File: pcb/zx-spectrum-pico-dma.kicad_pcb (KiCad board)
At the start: 2 copper layers, 98.2 x 99.9 mm, 19 parts, among them J101 SWD, J102 Blippers, J103 Z80 Data Bus, J104 Z80 Address Bus, J105 Z80 Control Bus, J106 ZX Control, J107 OLED, J108 Spare GPIOs, Q101 PMBT2222A, SW101 BTN_RESET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

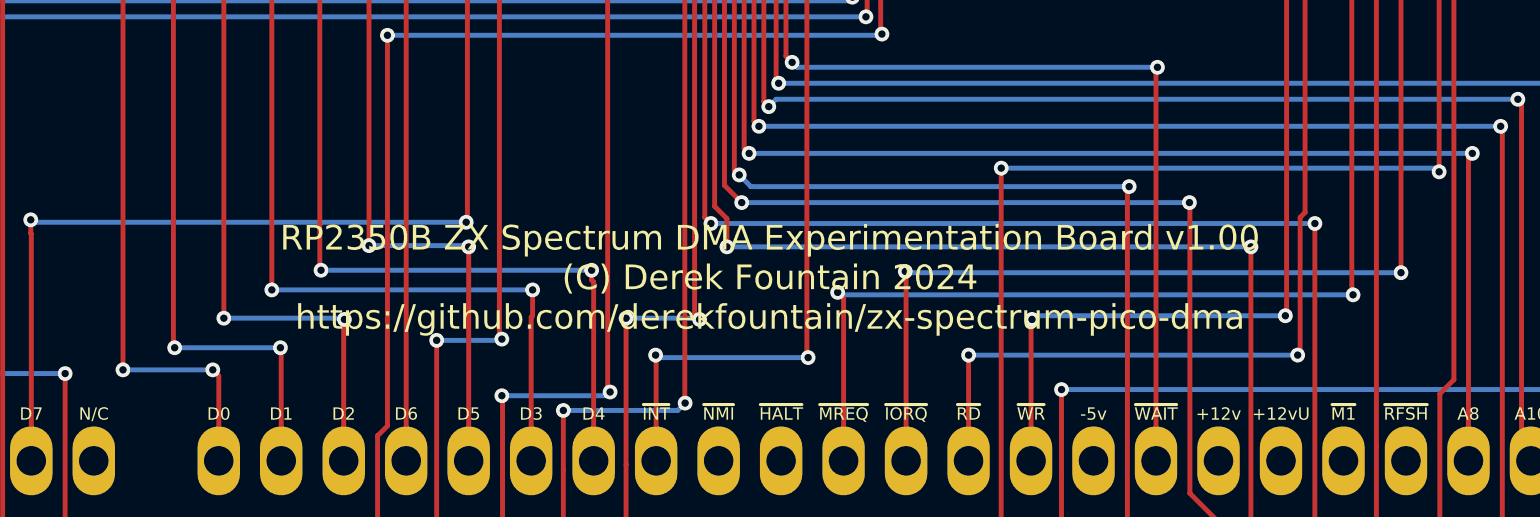
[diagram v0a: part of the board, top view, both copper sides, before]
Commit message: update schematic to reflect the revised RESET labelling
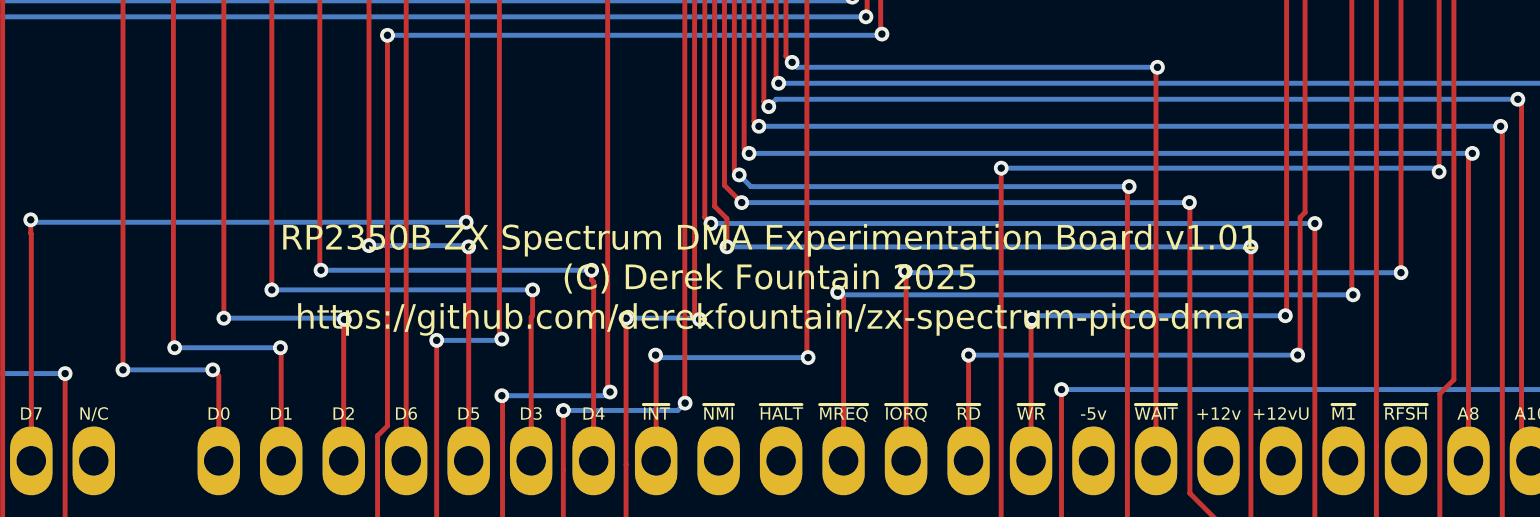
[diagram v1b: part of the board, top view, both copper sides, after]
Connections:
- net /RESET_Z80 renamed RESET_Z80
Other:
- board text added: "RP2350B ZX Spectrum DMA Experimentation Board v1.01 (C) Derek Fountain 2025 https://github.com/derekfountain/zx-spectrum-pico-dma"
- board text removed: "RP2350B ZX Spectrum DMA Experimentation Board v1.00 (C) Derek Fountain 2024 https://github.com/derekfountain/zx-spectrum-pico-dma"

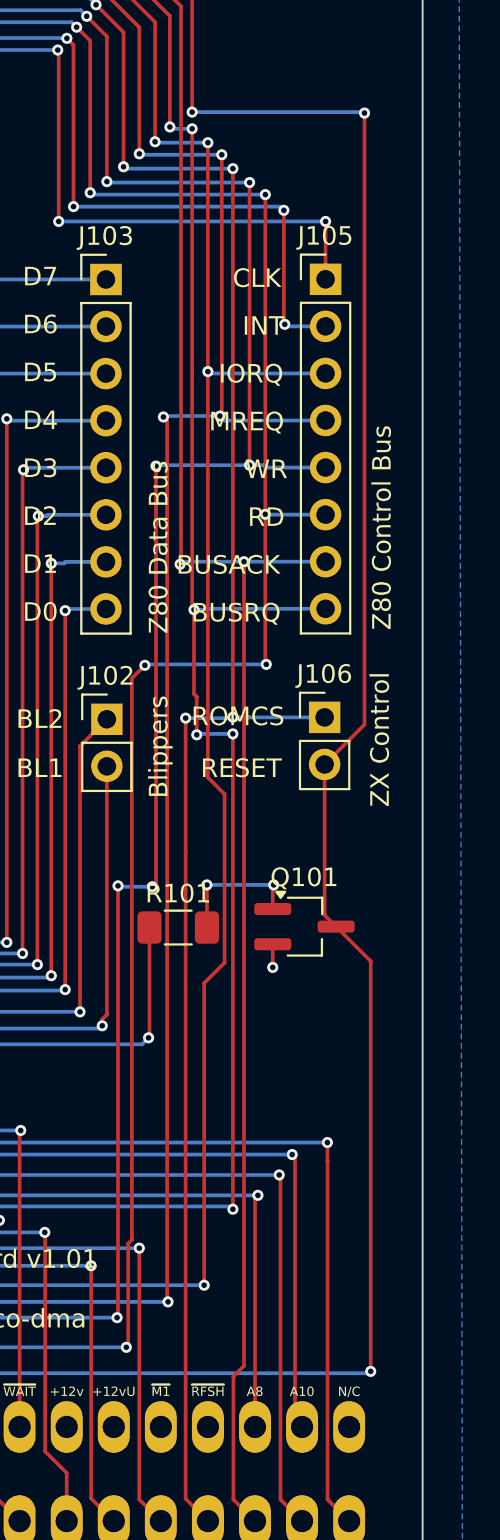
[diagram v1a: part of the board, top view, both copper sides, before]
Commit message: add M1 from edge connector to a pin, it's needed on the logic analyser so I need to make it available
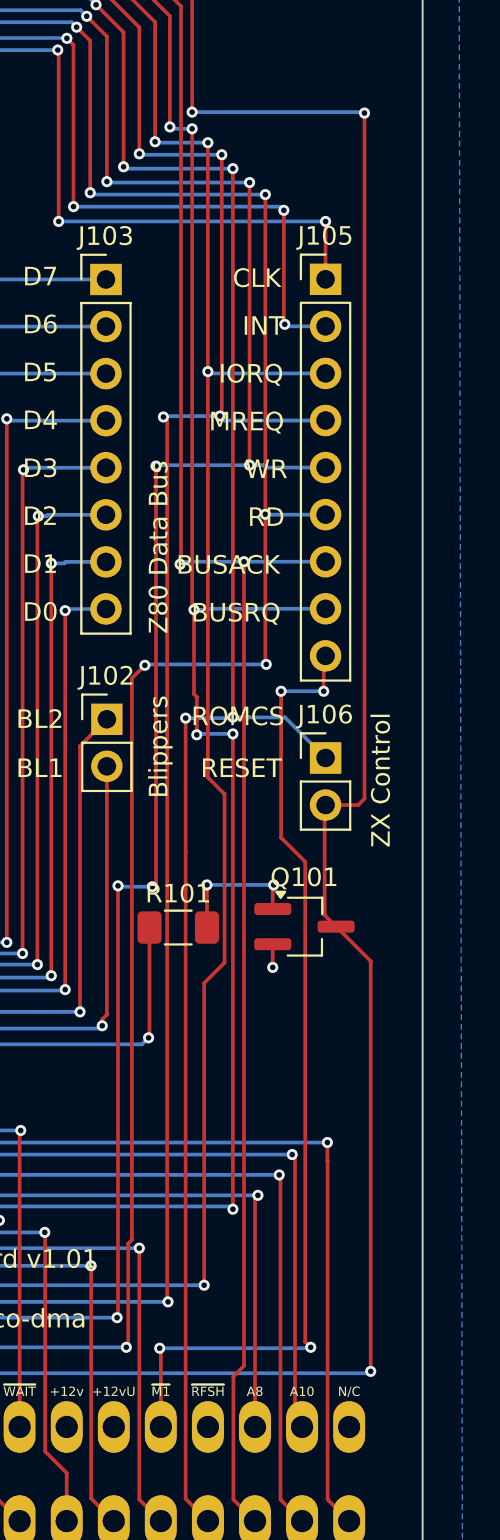
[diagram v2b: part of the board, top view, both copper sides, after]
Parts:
- J105: value Z80 Control Bus -> Conn_01x09; footprint Connector_PinHeader_2.54mm:PinHeader_1x08_P2.54mm_Vertical -> Connector_PinHeader_2.54mm:PinHeader_1x09_P2.54mm_Vertical
- moved J106 2.19 mm to (144.6, 108.8)
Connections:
- Z101 pad A24: unconnected-(Z101-~{M1}-PadA24) -> ZXM1
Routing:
- net ZXM1: track 0.00 -> 52.8 mm, vias 0 -> 4
- net ZXRESET: track 169.7 -> 170.7 mm
- net ZXROMCS: track 129.7 -> 130.7 mm
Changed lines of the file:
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@@
 	(paper "A4")
 	(title_block
-		(date "2024-11-29")
+		(date "2025-03-14")
 	)
 	(layers
@@
 	(net 68 "unconnected-(Z101-NC-PadA28)")
 	(net 69 "/GPIO39")
-	(net 70 "unconnected-(Z101-~{M1}-PadA24)")
+	(net 70 "ZXM1")
 	(net 71 "unconnected-(Z101-~{NMI}-PadA14)")
 	(net 72 "unconnected-(Z101-~{HALT}-PadA15)")
@@
 	(footprint "Connector_PinHeader_2.54mm:PinHeader_1x02_P2.54mm_Vertical"
 		(layer "F.Cu")
-		(at 144.5 106.66)
+		(at 144.55 108.85)
 		(descr "Through hole straight pin header, 1x02, 2.54mm pitch, single row")
 		(tags "Through hole pin header THT 1x02 2.54mm single row")
@@
 			)
 			(remove_unused_layers no)
-			(net 70 "unconnected-(Z101-~{M1}-PadA24)")
+			(net 70 "ZXM1")
 			(pinfunction "~{M1}")
-			(pintype "input+no_connect")
+			(pintype "input")
 		)
 		(pad "A25" thru_hole oval
@@
 		)
 	)
-	(footprint "Connector_PinHeader_2.54mm:PinHeader_1x08_P2.54mm_Vertical"
+	(footprint "Connector_PinHeader_2.54mm:PinHeader_1x09_P2.54mm_Vertical"
 		(layer "F.Cu")
 		(at 144.55 83.02)
-		(descr "Through hole straight pin header, 1x08, 2.54mm pitch, single row")
-		(tags "Through hole pin header THT 1x08 2.54mm single row")
+		(descr "Through hole straight pin header, 1x09, 2.54mm pitch, single row")
+		(tags "Through hole pin header THT 1x09 2.54mm single row")
 		(property "Reference" "J105"
 			(at 0 -2.33 0)
@@
 			)
 		)
-		(property "Value" "Z80 Control Bus"
-			(at 3.05 13.4 90)
-			(layer "F.SilkS")
+		(property "Value" "Conn_01x09"
+			(at 0 22.65 0)
+			(layer "F.Fab")
 			(effects
 				(font
@@
 			)
 		)
-		(property "Footprint" "Connector_PinHeader_2.54mm:PinHeader_1x08_P2.54mm_Vertical"
+		(property "Footprint" "Connector_PinHeader_2.54mm:PinHeader_1x09_P2.54mm_Vertical"
 			(at 0 0 0)
 			(unlocked yes)
@@
 			)
 		)
-		(property "Description" "Generic connector, single row, 01x08, script generated (kicad-library-utils/schlib/autogen/connector/)"
+		(property "Description" "Generic connector, single row, 01x09, script generated (kicad-library-utils/schlib/autogen/connector/)"
 			(at 0 0 0)
 			(unlocked yes)
@@
 		(fp_line
 			(start -1.33 1.27)
-			(end -1.33 19.11)
+			(end -1.33 21.65)
 			(stroke
 				(width 0.12)
@@
 		)
 		(fp_line
-			(start -1.33 19.11)
-			(end 1.33 19.11)
+			(start -1.33 21.65)
+			(end 1.33 21.65)
 			(stroke
 				(width 0.12)
@@
 		(fp_line
 			(start 1.33 1.27)
-			(end 1.33 19.11)
+			(end 1.33 21.65)
 			(stroke
 				(width 0.12)
@@
 		(fp_line
 			(start -1.8 -1.8)
-			(end -1.8 19.55)
+			(end -1.8 22.1)
 			(stroke
 				(width 0.05)
@@
 		)
 		(fp_line
-			(start -1.8 19.55)
-			(end 1.8 19.55)
+			(start -1.8 22.1)
+			(end 1.8 22.1)
 			(stroke
 				(width 0.05)
@@
 		)
 		(fp_line
-			(start 1.8 19.55)
+			(start 1.8 22.1)
 			(end 1.8 -1.8)
 			(stroke
@@
 		)
 		(fp_line
-			(start -1.27 19.05)
+			(start -1.27 21.59)
 			(end -1.27 -0.635)
 			(stroke
@@
 		(fp_line
 			(start 1.27 -1.27)
-			(end 1.27 19.05)
+			(end 1.27 21.59)
 			(stroke
 				(width 0.1)
@@
 		)
 		(fp_line
-			(start 1.27 19.05)
-			(end -1.27 19.05)
+			(start 1.27 21.59)
+			(end -1.27 21.59)
 			(stroke
 				(width 0.1)
@@
 		)
 		(fp_text user "${REFERENCE}"
-			(at 0 8.89 90)
+			(at 0 10.16 90)
 			(layer "F.Fab")
 			(effects
@@
 			(pintype "passive")
 		)
-		(model "${KICAD8_3DMODEL_DIR}/Connector_PinHeader_2.54mm.3dshapes/PinHeader_1x08_P2.54mm_Vertical.wrl"
+		(pad "9" thru_hole oval
+			(at 0 20.32)
+			(size 1.7 1.7)
+			(drill 1)
+			(layers "*.Cu" "*.Mask" "In1.Cu" "In2.Cu" "In3.Cu" "In4.Cu" "In5.Cu" "In6.Cu"
+				"In7.Cu" "In8.Cu" "In9.Cu" "In10.Cu" "In11.Cu" "In12.Cu" "In13.Cu" "In14.Cu"
+				"In15.Cu" "In16.Cu" "In17.Cu" "In18.Cu" "In19.Cu" "In20.Cu" "In21.Cu"
+				"In22.Cu" "In23.Cu" "In24.Cu" "In25.Cu" "In26.Cu" "In27.Cu" "In28.Cu"
+				"In29.Cu" "In30.Cu"
+			)
+			(remove_unused_layers no)
+			(net 70 "ZXM1")
+			(pinfunction "Pin_9")
+			(pintype "passive")
+		)
+		(model "${KICAD8_3DMODEL_DIR}/Connector_PinHeader_2.54mm.3dshapes/PinHeader_1x09_P2.54mm_Vertical.wrl"
 			(offset
 				(xyz 0 0 0)
@@
 	)
 	(segment
+		(start 146.31 111.39)
+		(end 144.55 111.39)
+		(width 0.2)
+		(layer "F.Cu")
+		(net 42)
+	)
+	(segment
 		(start 144.5 117.33)
 		(end 145.12 117.95)
@@
 	)
 	(segment
-		(start 146.65 107.05)
-		(end 144.5 109.2)
+		(start 144.55 111.39)
+		(end 144.5 111.44)
 		(width 0.2)
 		(layer "F.Cu")
@@
 	)
 	(segment
-		(start 134.8 65.2)
-		(end 137.35 67.75)
+		(start 146.65 111.05)
+		(end 146.31 111.39)
 		(width 0.2)
 		(layer "F.Cu")
@@
 	)
 	(segment
-		(start 137.35 67.75)
-		(end 137.35 74)
+		(start 146.65 74.05)
+		(end 146.65 111.05)
 		(width 0.2)
 		(layer "F.Cu")
@@
 	)
 	(segment
-		(start 144.5 109.2)
-		(end 144.5 117.33)
+		(start 134.8 65.2)
+		(end 137.35 67.75)
+		(width 0.2)
+		(layer "F.Cu")
+		(net 42)
+	)
+	(segment
+		(start 137.35 67.75)
+		(end 137.35 74)
 		(width 0.2)
 		(layer "F.Cu")
@@
 	)
 	(segment
-		(start 92.05 64.8)
-		(end 92 64.75)
+		(start 144.5 111.44)
+		(end 144.5 117.33)
 		(width 0.2)
 		(layer "F.Cu")
@@
 	)
 	(segment
-		(start 146.65 74.05)
-		(end 146.65 107.05)
+		(start 92.05 64.8)
+		(end 92 64.75)
 		(width 0.2)
 		(layer "F.Cu")
@@
 	(segment
 		(start 140.41 106.66)
-		(end 144.5 106.66)
+		(end 142.36 106.66)
 		(width 0.2)
 		(layer "B.Cu")
@@
 	)
 	(segment
-		(start 139.55 106.65)
-		(end 140.4 106.65)
+		(start 113.95 75)
+		(end 113.85 75.1)
 		(width 0.2)
 		(layer "B.Cu")
@@
 	)
 	(segment
-		(start 113.95 75)
-		(end 113.85 75.1)
+		(start 142.36 106.66)
+		(end 144.55 108.85)
 		(width 0.2)
 		(layer "B.Cu")
@@
 	)
 	(segment
+		(start 139.55 106.65)
+		(end 140.4 106.65)
+		(width 0.2)
+		(layer "B.Cu")
+		(net 43)
+	)
+	(segment
 		(start 62.15 68.35)
 		(end 62.15 67.45)
@@
 		(net 69)
 	)
+	(segment
+		(start 143.45 114.45)
+		(end 142.15 113.15)
+		(width 0.2)
+		(layer "F.Cu")
+		(net 70)
+	)
+	(segment
+		(start 143.75 140.65)
+		(end 143.45 140.35)
+		(width 0.2)
+		(layer "F.Cu")
+		(net 70)
+	)
+	(segment
+		(start 143.45 140.35)
+		(end 143.45 114.45)
+		(width 0.2)
+		(layer "F.Cu")
+		(net 70)
+	)
+	(segment
+		(start 144.45 105.25)
+		(end 144.45 103.44)
+		(width 0.2)
+		(layer "F.Cu")
+		(net 70)
+	)
+	(segment
+		(start 135.662 140.762)
+		(end 135.6 140.7)
+		(width 0.2)
+		(layer "F.Cu")
+		(net 70)
+	)
+	(segment
+		(start 135.662 144.948)
+		(end 135.662 140.762)
+		(width 0.2)
+		(layer "F.Cu")
+		(net 70)
+	)
+	(segment
+		(start 142.15 113.15)
+		(end 142.15 105.25)
+		(width 0.2)
+		(layer "F.Cu")
+		(net 70)
+	)
+	(segment
+		(start 144.45 103.44)
+		(end 144.55 103.34)
+		(width 0.2)
+		(layer "F.Cu")
+		(net 70)
+	)
+	(via
+		(at 144.45 105.25)
+		(size 0.6)
+		(drill 0.3)
+		(layers "F.Cu" "B.Cu")
+		(net 70)
+	)
+	(via
+		(at 143.75 140.65)
+		(size 0.6)
+		(drill 0.3)
+		(layers "F.Cu" "B.Cu")
+		(net 70)
+	)
+	(via
+		(at 142.15 105.25)
+		(size 0.6)
+		(drill 0.3)
+		(layers "F.Cu" "B.Cu")
+		(net 70)
+	)
+	(via
+		(at 135.6 140.7)
+		(size 0.6)
+		(drill 0.3)
+		(layers "F.Cu" "B.Cu")
+		(net 70)
+	)
+	(segment
+		(start 142.15 105.25)
+		(end 144.45 105.25)
+		(width 0.2)
+		(layer "B.Cu")
+		(net 70)
+	)
+	(segment
+		(start 143.7 140.7)
+		(end 143.75 140.65)
+		(width 0.2)
+		(layer "B.Cu")
+		(net 70)
+	)
+	(segment
+		(start 135.6 140.7)
+		(end 143.7 140.7)
+		(width 0.2)
+		(layer "B.Cu")
+		(net 70)
+	)
 	(zone

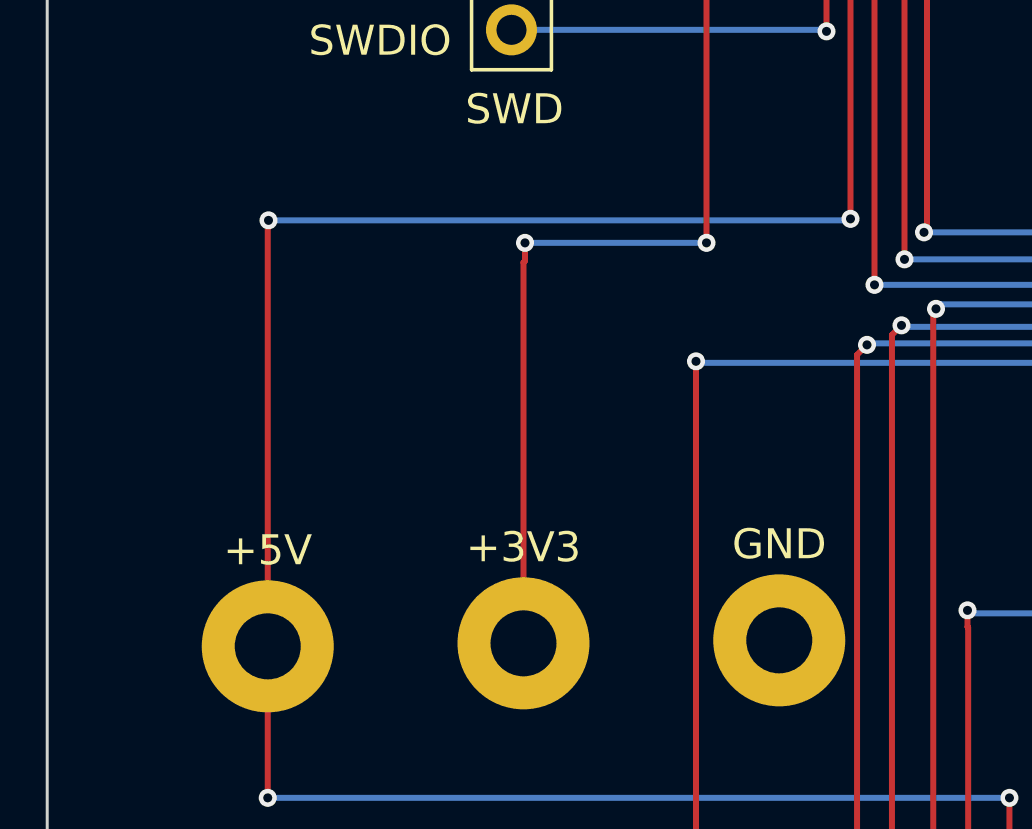
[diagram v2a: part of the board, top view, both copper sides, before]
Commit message: add a 3-pin supplies header, the mounting points aren't easy to attach a clip to
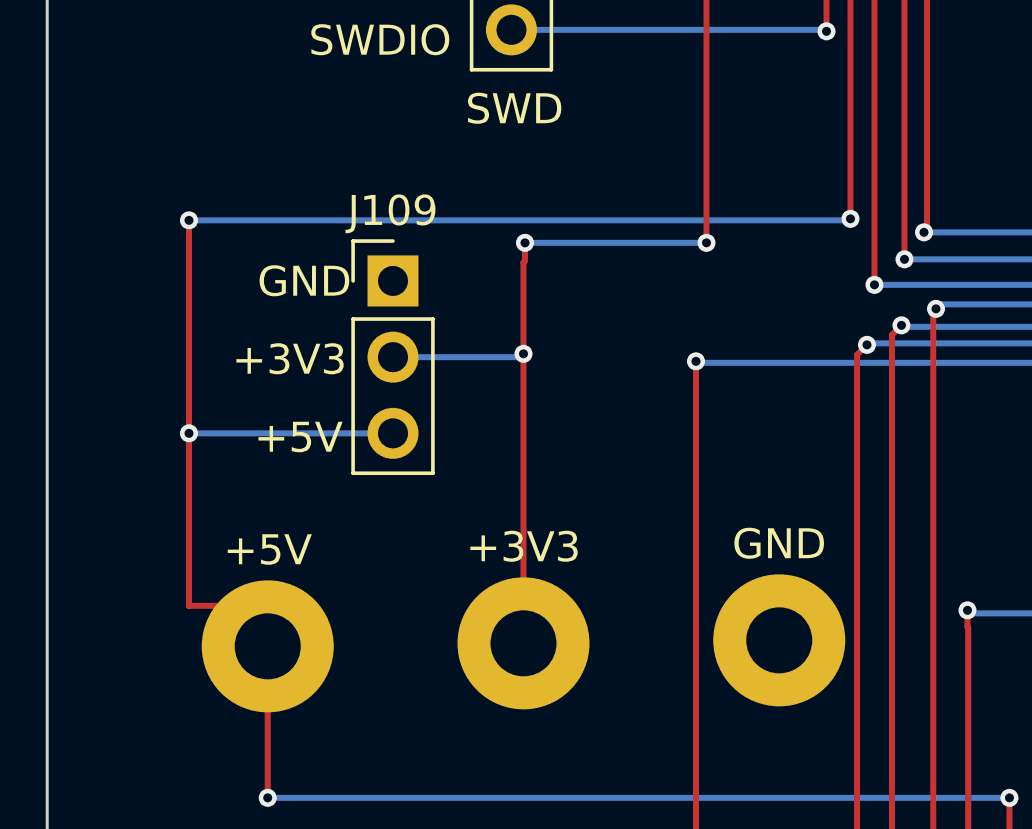
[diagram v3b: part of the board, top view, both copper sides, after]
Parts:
- added J109: Conn_01x03, Connector_PinHeader_2.54mm:PinHeader_1x03_P2.54mm_Vertical, F.Cu at (63.1, 124.2)
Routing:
- net +5V: track 103.4 -> 120.4 mm, vias 5 -> 6
- net +3V3: track 110.0 -> 114.4 mm, vias 5 -> 6
